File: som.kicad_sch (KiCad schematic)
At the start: 27 parts, among them M2 jetson-orin-nx/nano-module

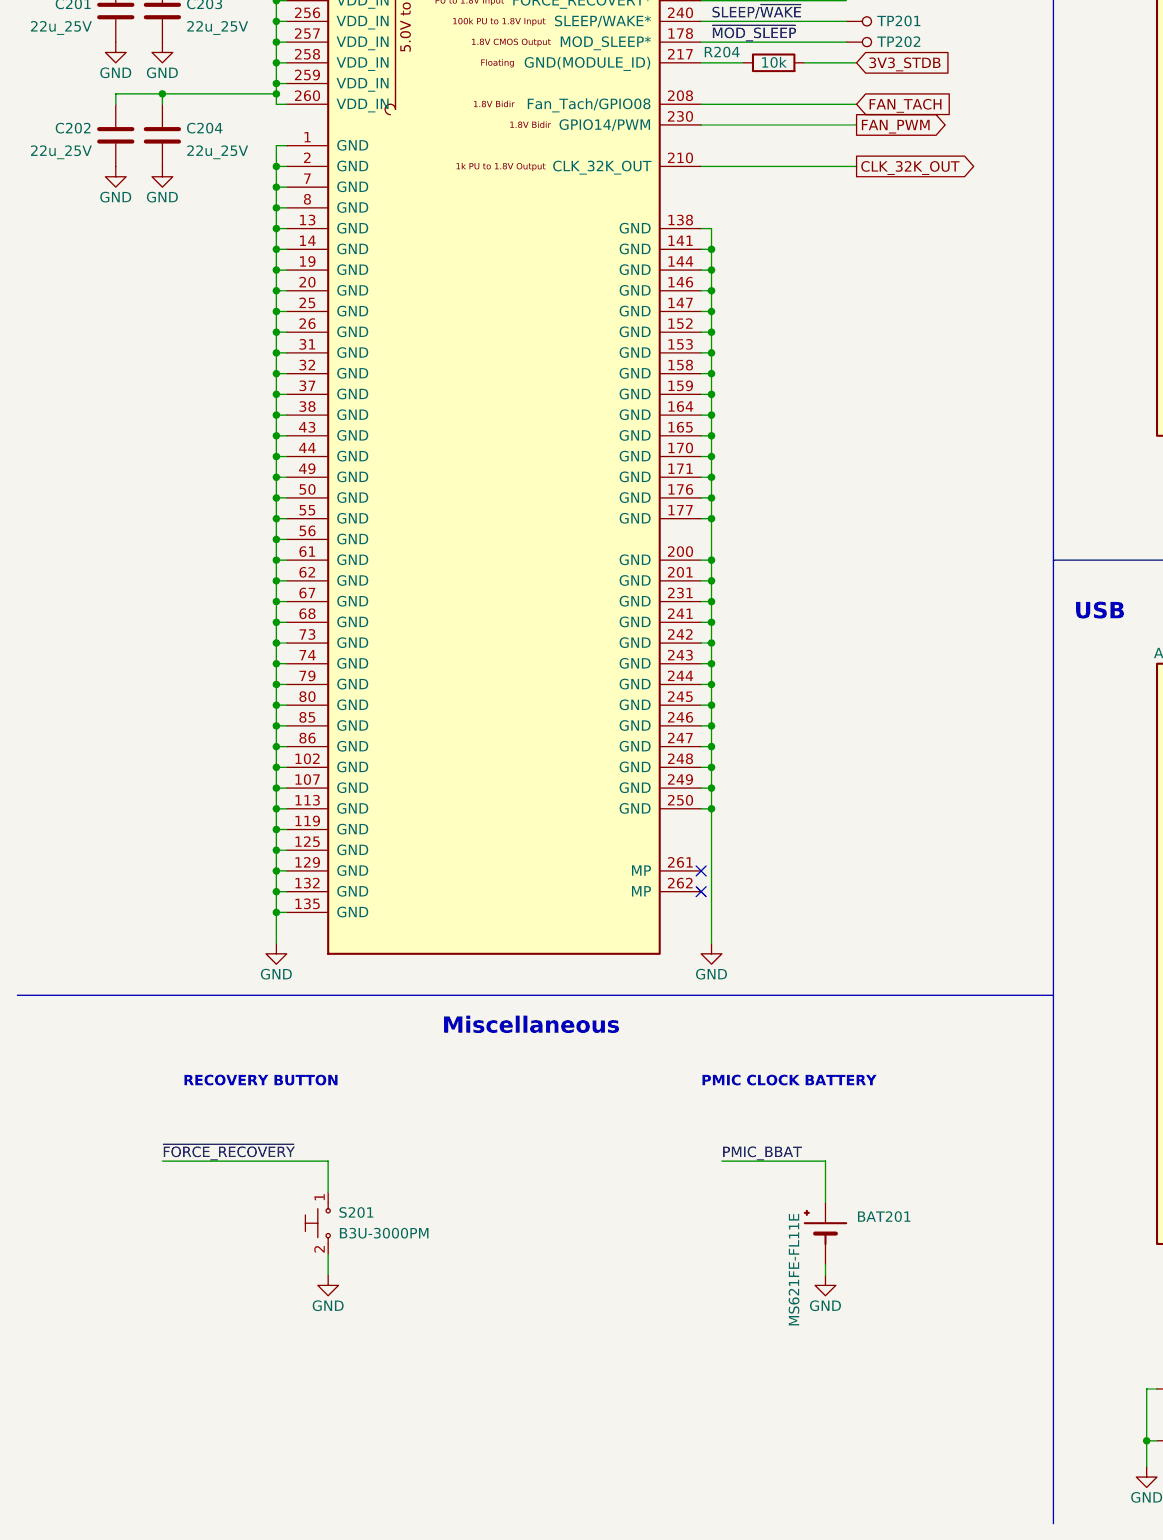
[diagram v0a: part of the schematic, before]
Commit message: Add 3V3 translator to 32kHz clock
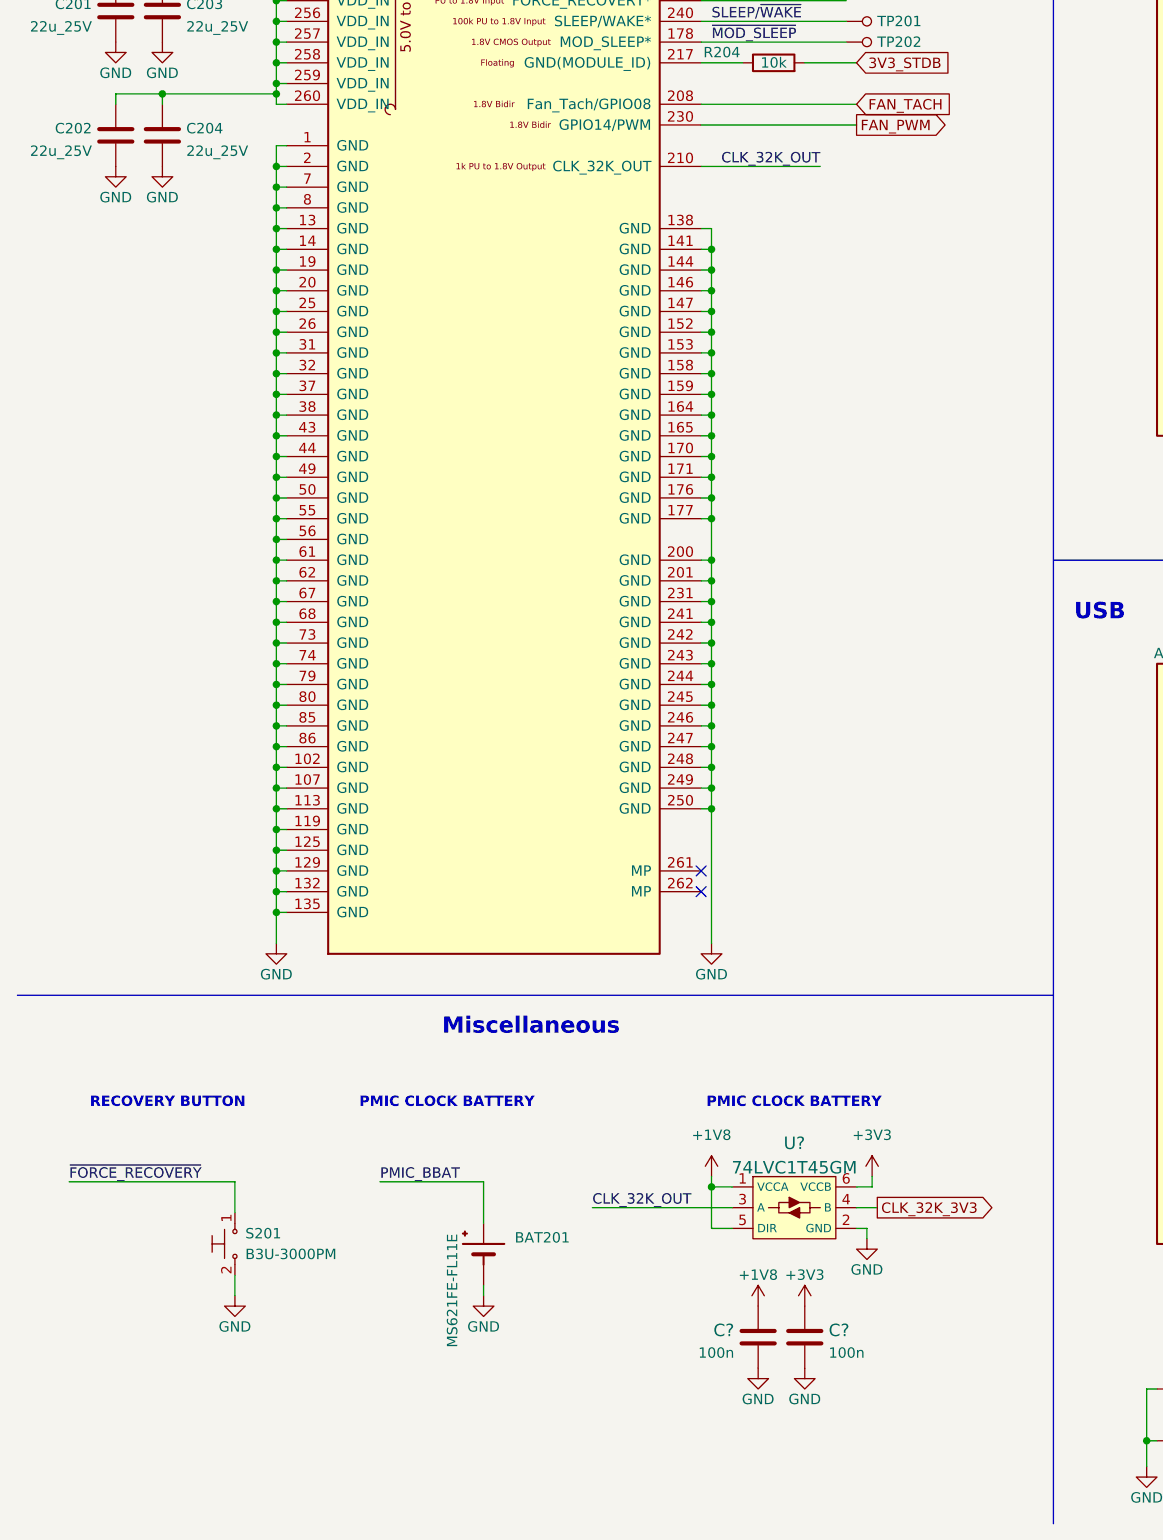
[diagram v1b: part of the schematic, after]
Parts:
- added C? (x2): C_100n_0402, antmicro-footprints:0402-cap, symbol antmicroCapacitors0402:C_100n_0402
- added U?: 74LVC1T45GM, antmicro-footprints:SOT-886, symbol antmicroLogicTranslatorsLevelShifters:74LVC1T45GM
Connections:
- net CLK_32K_OUT: now also U?.3 (A)
- net GND: now also C?.2, C?.2, U?.2 (GND)
- new net +1V8: C?.1, U?.1 (VCCA), U?.5 (DIR)
- new net +3V3: C?.1, U?.6 (VCCB)
- new net CLK_32K_3V3: U?.4 (B)
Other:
- moved on the sheet: BAT201, S201

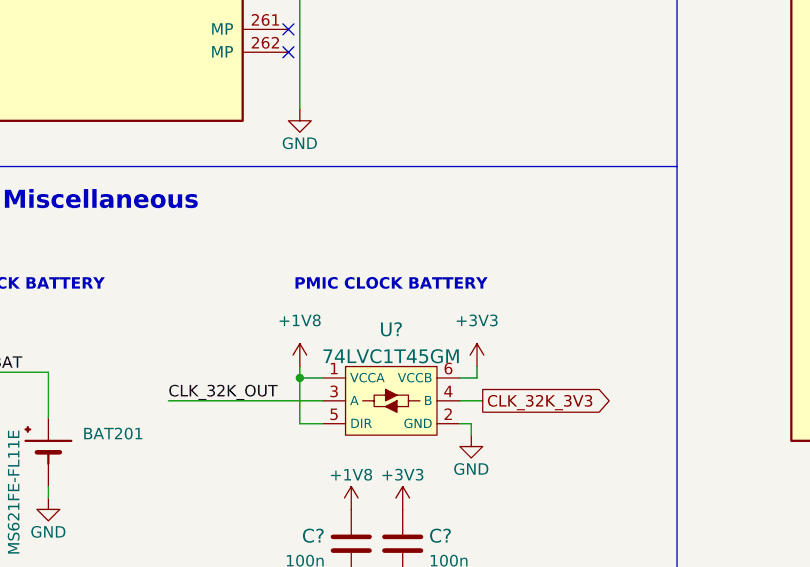
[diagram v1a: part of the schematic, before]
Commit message: Change text item to properly describe clock buffer
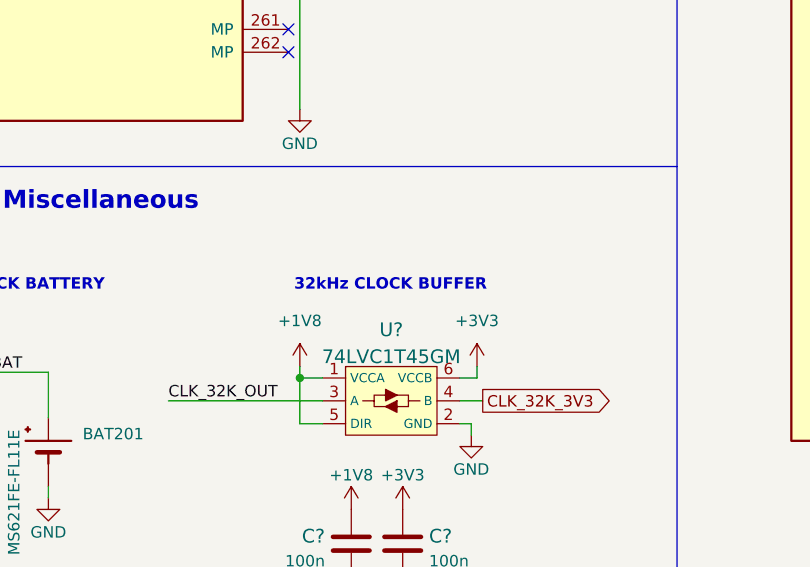
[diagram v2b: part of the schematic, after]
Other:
- note added: "32kHz CLOCK BUFFER"
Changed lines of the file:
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@@
     (effects (font (size 2 2) (thickness 0.508) bold) (justify left bottom))
   )
-  (text "PMIC CLOCK BATTERY" (at 97.155 232.41 0)
+  (text "32kHz CLOCK BUFFER" (at 97.155 232.41 0)
     (effects (font (size 1.27 1.27) (thickness 0.254) bold) (justify left bottom))
   )

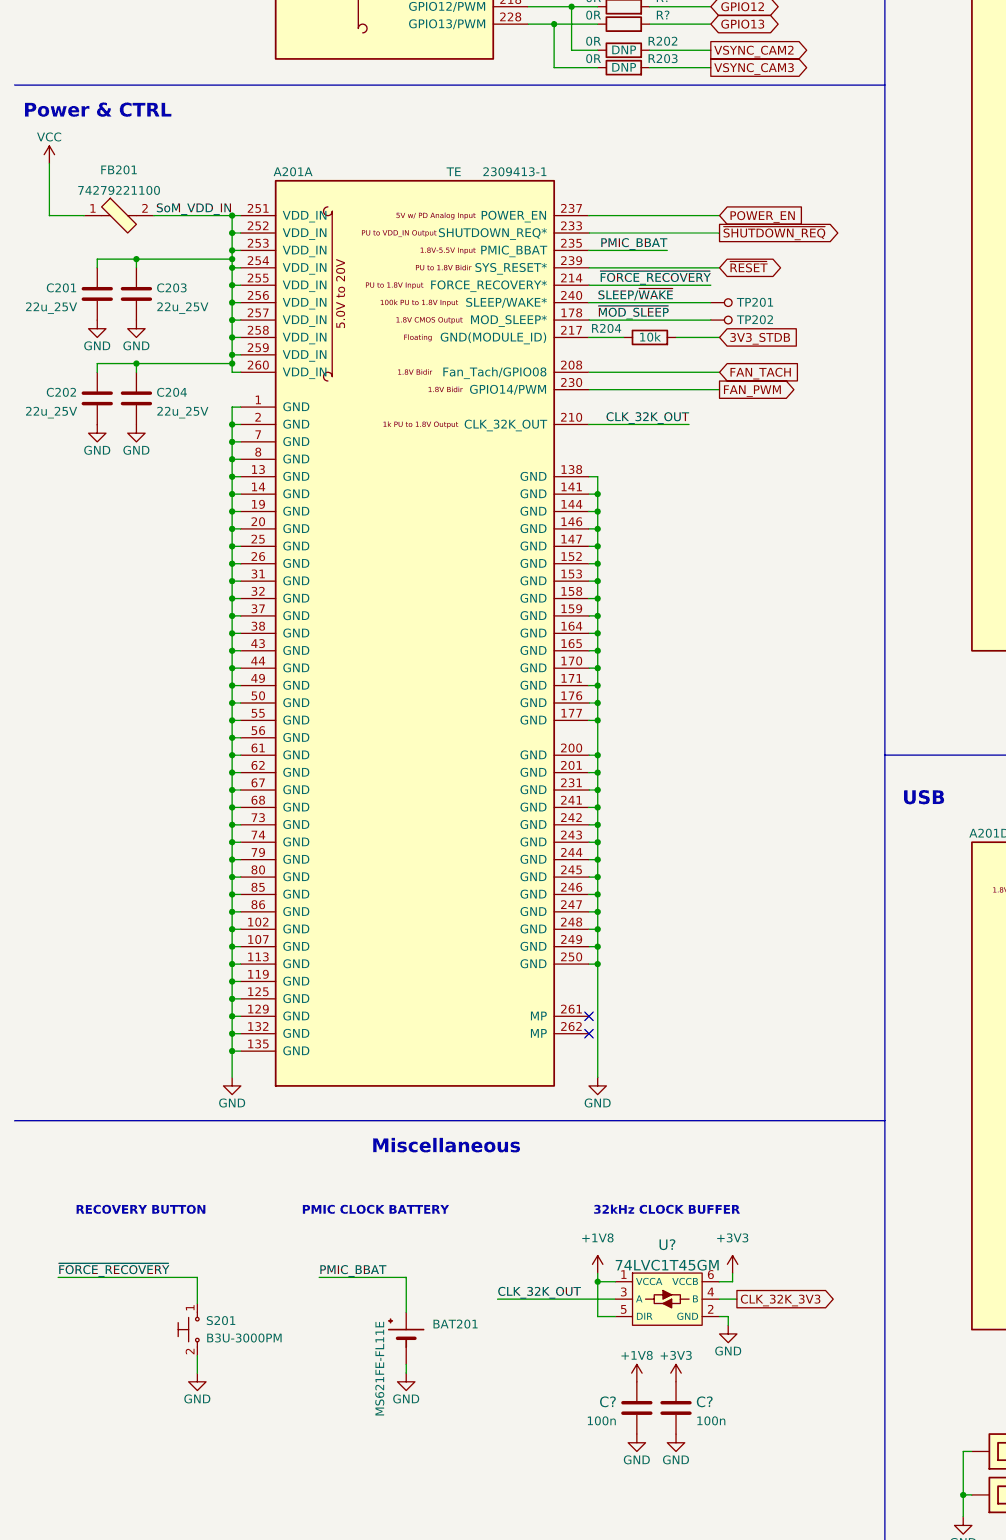
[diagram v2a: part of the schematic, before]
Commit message: Update SoM symbol and improve readability around SoM CTRL signals
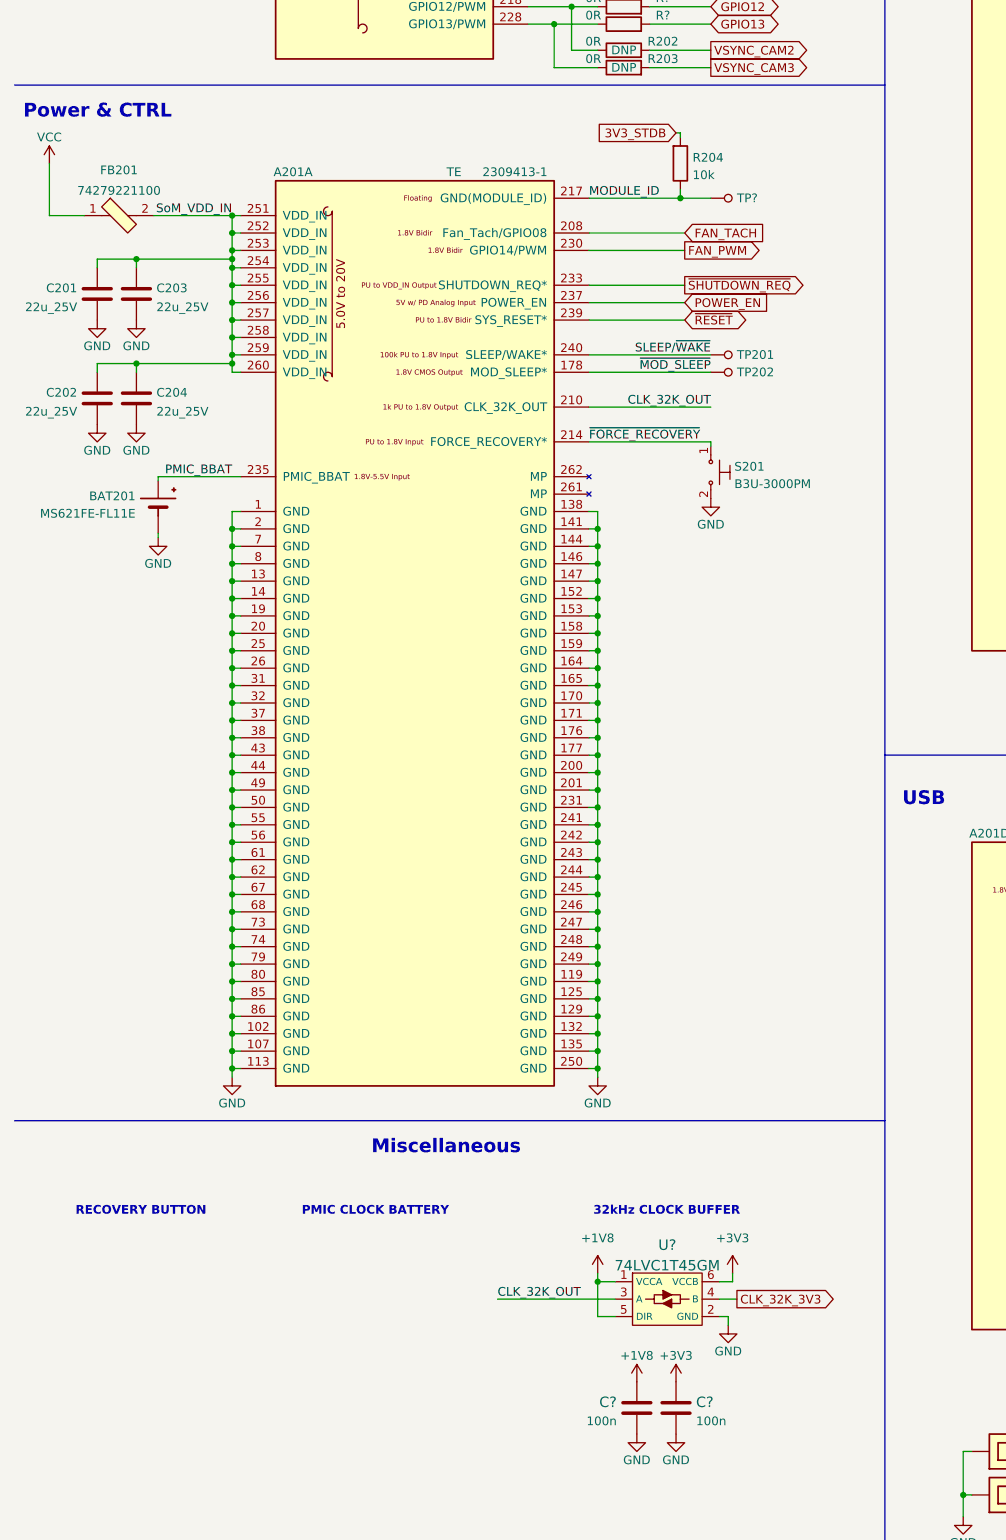
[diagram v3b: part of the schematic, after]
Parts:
- added TP?: TP_SMD_0_75MM, antmicro-footprints:Testpoint_smd_0_75mm, symbol antmicroTestPoints:TP_SMD_0_75MM
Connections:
- net MODULE_ID: now reaches A201.217 (GND(MODULE_ID)), R204.1
- net MODULE_ID: now also TP?.1
- no-connect marks 13 -> 11
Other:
- moved on the sheet: BAT201, R204, S201, TP201, TP202

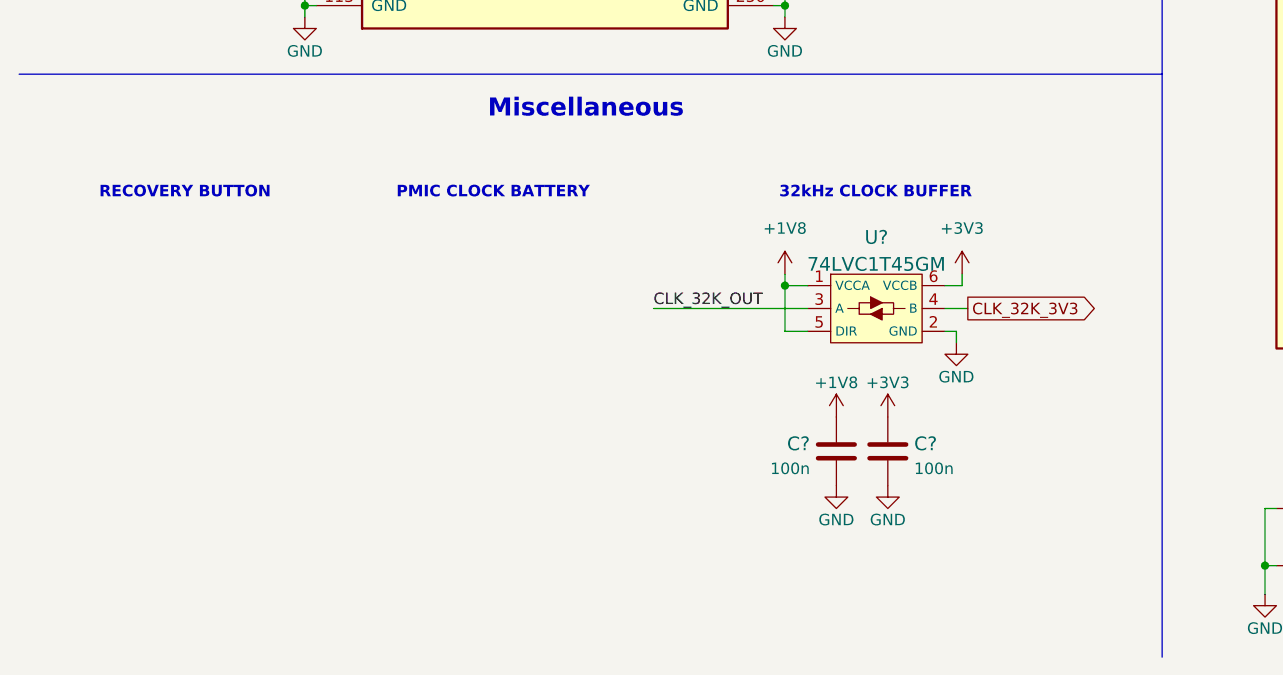
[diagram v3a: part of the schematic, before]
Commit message: Clear miscellaneous section in som sheet
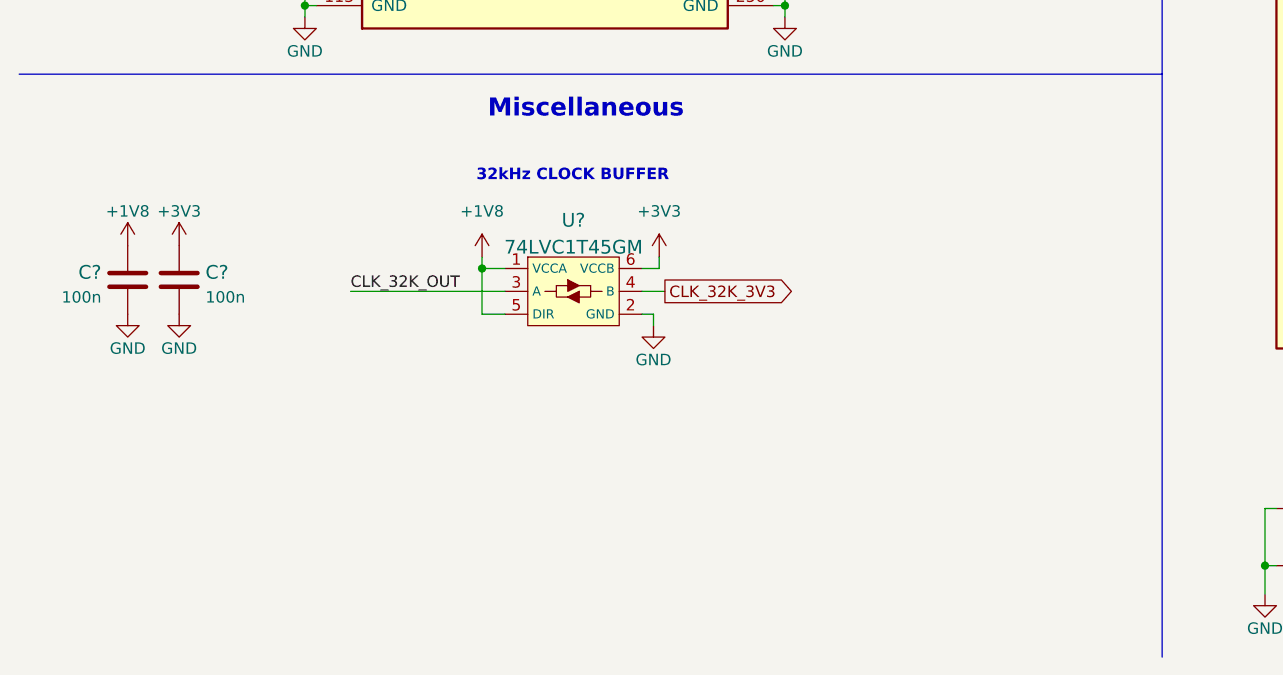
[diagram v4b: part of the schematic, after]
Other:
- note removed: "PMIC CLOCK BATTERY"
- note removed: "RECOVERY BUTTON"
- moved on the sheet: C?, U?
